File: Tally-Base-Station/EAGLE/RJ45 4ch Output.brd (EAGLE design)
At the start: 84.8 x 26.7 mm, 9 parts, among them J1 CAMOUT1, J2 CAMOUT2, J3 CAMOUT3, J4 CAMOUT4

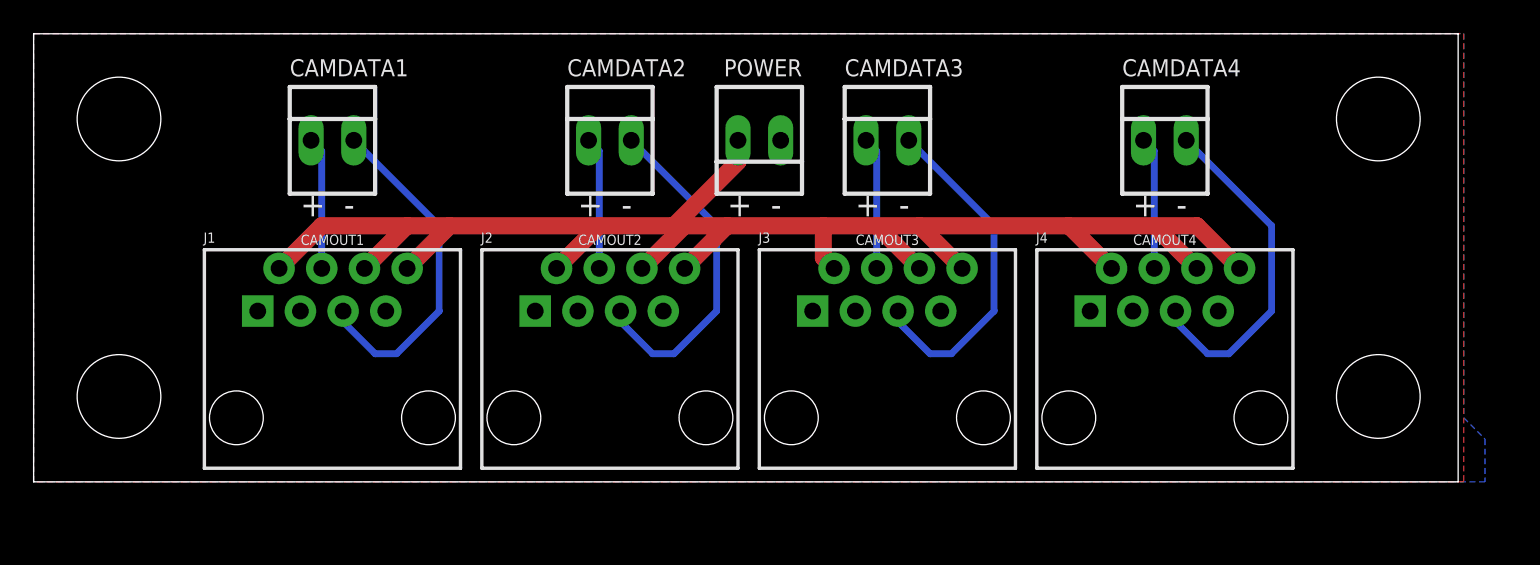
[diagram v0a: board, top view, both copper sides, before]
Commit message: Standardize RS485 pinouts, update RJ45 pinouts.
Fix pin assignments for the RS485 interconnects to standardize on pin1 = data-.
Update the RJ45 breakouts to be mostly pin compatible with DMX over ethernet wiring standard (using pin 5/6 for V+)
Create an XLR RS485 breakout option for wiring cameras together using 3pin DMX cables
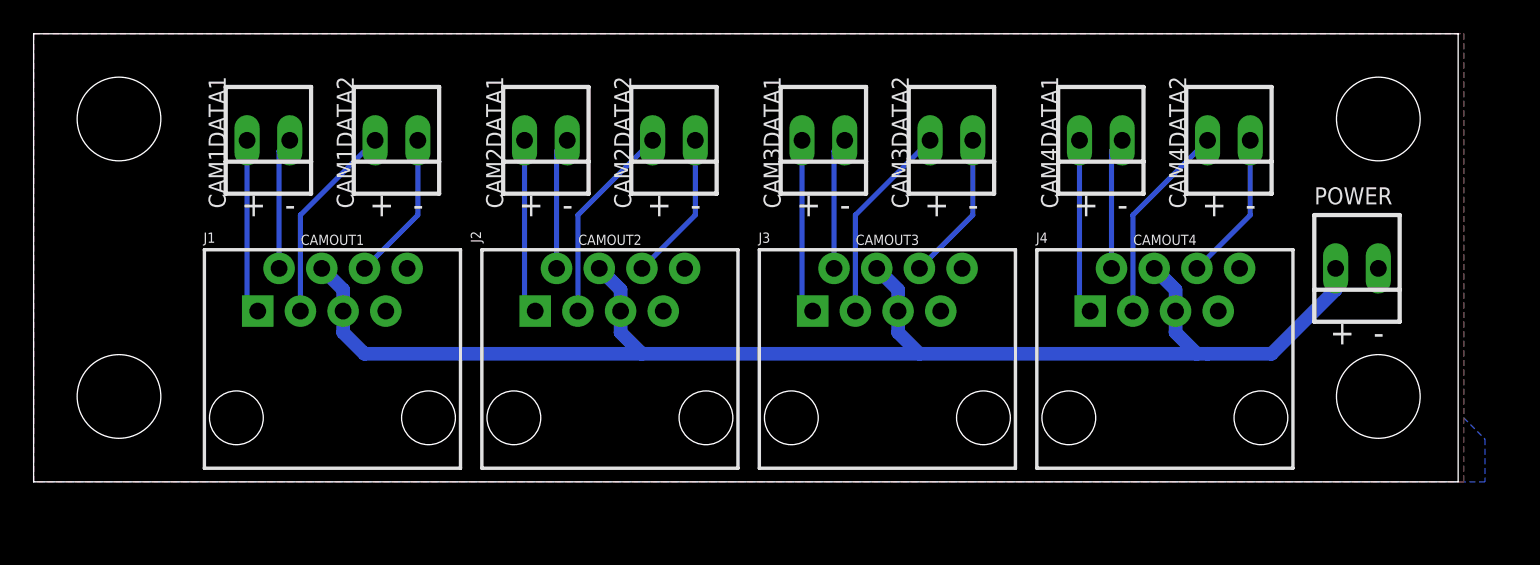
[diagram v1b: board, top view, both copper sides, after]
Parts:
- removed CAMDATA1, CAMDATA2, CAMDATA3, CAMDATA4: 22-23-2021, con-molex:22-23-2021
- added CAM1DATA1, CAM1DATA2, CAM2DATA1, CAM2DATA2, CAM3DATA1, CAM3DATA2, CAM4DATA1, CAM4DATA2: 22-23-2021, con-molex:22-23-2021
- moved POWER 36.4 mm to (78.7, 12.7)
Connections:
- removed net C1DATA+: CAMDATA1.1, J1.4
- removed net C1DATA-: CAMDATA1.2, J1.5
- removed net C2DATA+: CAMDATA2.1, J2.4
- removed net C2DATA-: CAMDATA2.2, J2.5
- removed net C3DATA+: CAMDATA3.1, J3.4
- removed net C3DATA-: CAMDATA3.2, J3.5
- removed net C4DATA+: CAMDATA4.1, J4.4
- removed net C4DATA-: CAMDATA4.2, J4.5
- new net C1DATA1+: CAM1DATA1.2, J1.1
- new net C1DATA1-: CAM1DATA1.1, J1.2
- new net C1DATA2+: CAM1DATA2.2, J1.3
- new net C1DATA2-: CAM1DATA2.1, J1.6
- new net C2DATA1+: CAM2DATA1.2, J2.1
- new net C2DATA1-: CAM2DATA1.1, J2.2
- new net C2DATA2+: CAM2DATA2.2, J2.3
- new net C2DATA2-: CAM2DATA2.1, J2.6
- new net C3DATA1+: CAM3DATA1.2, J3.1
- new net C3DATA1-: CAM3DATA1.1, J3.2
- new net C3DATA2+: CAM3DATA2.2, J3.3
- new net C3DATA2-: CAM3DATA2.1, J3.6
- new net C4DATA1+: CAM4DATA1.2, J4.1
- new net C4DATA1-: CAM4DATA1.1, J4.2
- new net C4DATA2+: CAM4DATA2.2, J4.3
- new net C4DATA2-: CAM4DATA2.1, J4.6
- net GND: now also J1.8, J2.8, J3.8, J4.8; no longer J1.1, J1.3, J2.1, J2.3, J3.1, J3.3, J4.1, J4.3
- net VCC: now also J1.4, J1.5, J2.4, J2.5, J3.4, J3.5, J4.4, J4.5; no longer J1.2, J1.6, J1.8, J2.2, J2.6, J2.8, J3.2, J3.6, J3.8, J4.2, J4.6, J4.8
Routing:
- net C4DATA-: track 20.5 -> 0.00 mm
- net C2DATA-: track 20.5 -> 0.00 mm
- net C3DATA-: track 20.5 -> 0.00 mm
- net C1DATA-: track 20.5 -> 0.00 mm
- net VCC: track 101.0 -> 85.2 mm
- net C3DATA2+: track 0.00 -> 12.0 mm
- net C2DATA2+: track 0.00 -> 12.0 mm
- net C1DATA2+: track 0.00 -> 12.0 mm
- net C4DATA2+: track 0.00 -> 12.0 mm
- net C4DATA1+: track 0.00 -> 10.4 mm
- net C1DATA1+: track 0.00 -> 10.4 mm
- net C3DATA1+: track 0.00 -> 10.4 mm
- net C2DATA1+: track 0.00 -> 10.4 mm
- net C3DATA2-: track 0.00 -> 8.94 mm
- net C1DATA2-: track 0.00 -> 8.94 mm
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
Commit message: Update RJ45 boards to use RJHSE Amphenol jacks
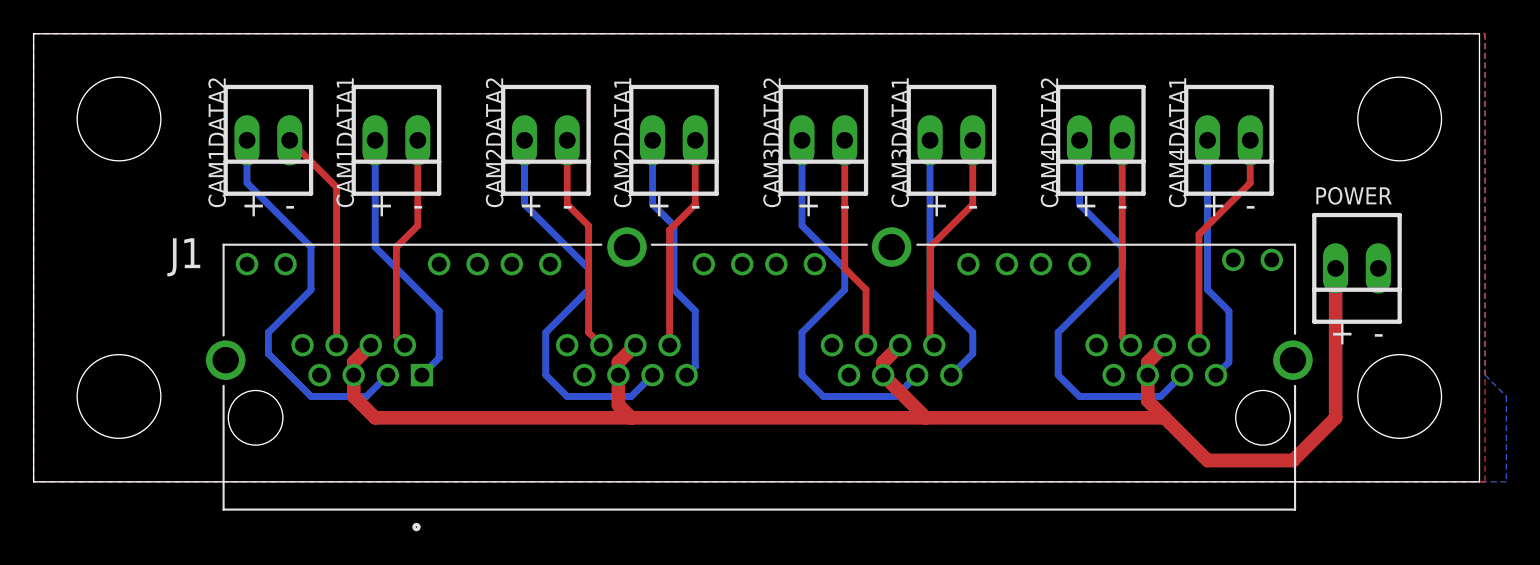
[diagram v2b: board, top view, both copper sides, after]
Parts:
- removed J2: CAMOUT2, SparkFun-Connectors:RJ45-8
- removed J3: CAMOUT3, SparkFun-Connectors:RJ45-8
- removed J4: CAMOUT4, SparkFun-Connectors:RJ45-8
- J1: value CAMOUT1 -> RJHSE-5381-04; device SparkFun-Connectors:RJ45-8 -> RJHSE-5381-04:AMPHENOL_RJHSE-5381-04
- moved J1 25.4 mm to (43.2, 3.81)
- moved CAM4DATA1 7.62 mm to (71.1, 20.3)
- moved CAM4DATA2 7.62 mm to (63.5, 20.3)
- moved CAM2DATA1 7.62 mm to (38.1, 20.3)
- moved CAM2DATA2 7.62 mm to (30.5, 20.3)
- moved CAM1DATA1 7.62 mm to (21.6, 20.3)
- moved CAM1DATA2 7.62 mm to (14.0, 20.3)
- moved CAM3DATA1 7.62 mm to (54.6, 20.3)
- moved CAM3DATA2 7.62 mm to (47.0, 20.3)
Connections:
- new net LED1A: J1.10
- new net LED1B: J1.12
- new net LED2A: J1.22
- new net LED2B: J1.24
- new net LED3A: J1.34
- new net LED3B: J1.36
- new net LED4A: J1.46
- new net LED4B: J1.48
- net C2DATA1+: now also J1.13; no longer J2.1
- net C2DATA1-: now also J1.14; no longer J2.2
- net C2DATA2+: now also J1.15; no longer J2.3
- net C2DATA2-: now also J1.18; no longer J2.6
- net C3DATA1+: now also J1.25; no longer J3.1
- net C3DATA1-: now also J1.26; no longer J3.2
- net C3DATA2+: now also J1.27; no longer J3.3
- net C3DATA2-: now also J1.30; no longer J3.6
- net C4DATA1+: now also J1.37; no longer J4.1
- net C4DATA1-: now also J1.38; no longer J4.2
- net C4DATA2+: now also J1.39; no longer J4.3
- net C4DATA2-: now also J1.42; no longer J4.6
- net GND: now also J1.11, J1.19, J1.20, J1.21, J1.23, J1.31, J1.32, J1.33, J1.35, J1.43, J1.44, J1.45, J1.47, J1.9, J1.S1, J1.S2, J1.S3, J1.S4; no longer J2.7, J2.8, J3.7, J3.8, J4.7, J4.8
- net VCC: now also J1.16, J1.17, J1.28, J1.29, J1.40, J1.41; no longer J2.4, J2.5, J3.4, J3.5, J4.4, J4.5
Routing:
- net C4DATA2+: track 12.0 -> 25.0 mm
- net C1DATA2+: track 12.0 -> 24.0 mm
- net C2DATA2+: track 12.0 -> 24.0 mm
- net C3DATA2+: track 12.0 -> 24.0 mm
- net C4DATA1-: track 7.88 -> 13.5 mm
- net C1DATA1+: track 10.4 -> 16.0 mm
- net C3DATA1-: track 7.88 -> 13.3 mm
- net C3DATA1+: track 10.4 -> 15.6 mm
- net C1DATA1-: track 7.88 -> 12.9 mm
- net C2DATA1-: track 7.88 -> 12.8 mm
- net C2DATA1+: track 10.4 -> 15.2 mm
- net C1DATA2-: track 8.94 -> 13.3 mm
- net C4DATA1+: track 10.4 -> 14.8 mm
- net VCC: track 85.2 -> 89.4 mm
- net C2DATA2-: track 8.94 -> 13.0 mm
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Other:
- board size 84.8 x 26.7 mm -> 86 x 26.7 mm
